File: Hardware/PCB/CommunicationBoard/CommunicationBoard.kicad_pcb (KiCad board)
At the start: 4 copper layers, 60 x 60 mm, 46 parts, among them J1 SWD, J2 Conn_01x07, J3 Conn_01x07, J4 Conn_01x07, J6 USB_C_Receptacle_USB2.0, J7 TWELITER, SW1 nRF_RESET, SW2 nRF_DFU, SW3 TWE_CLEAR, SW4 TWE_RESET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

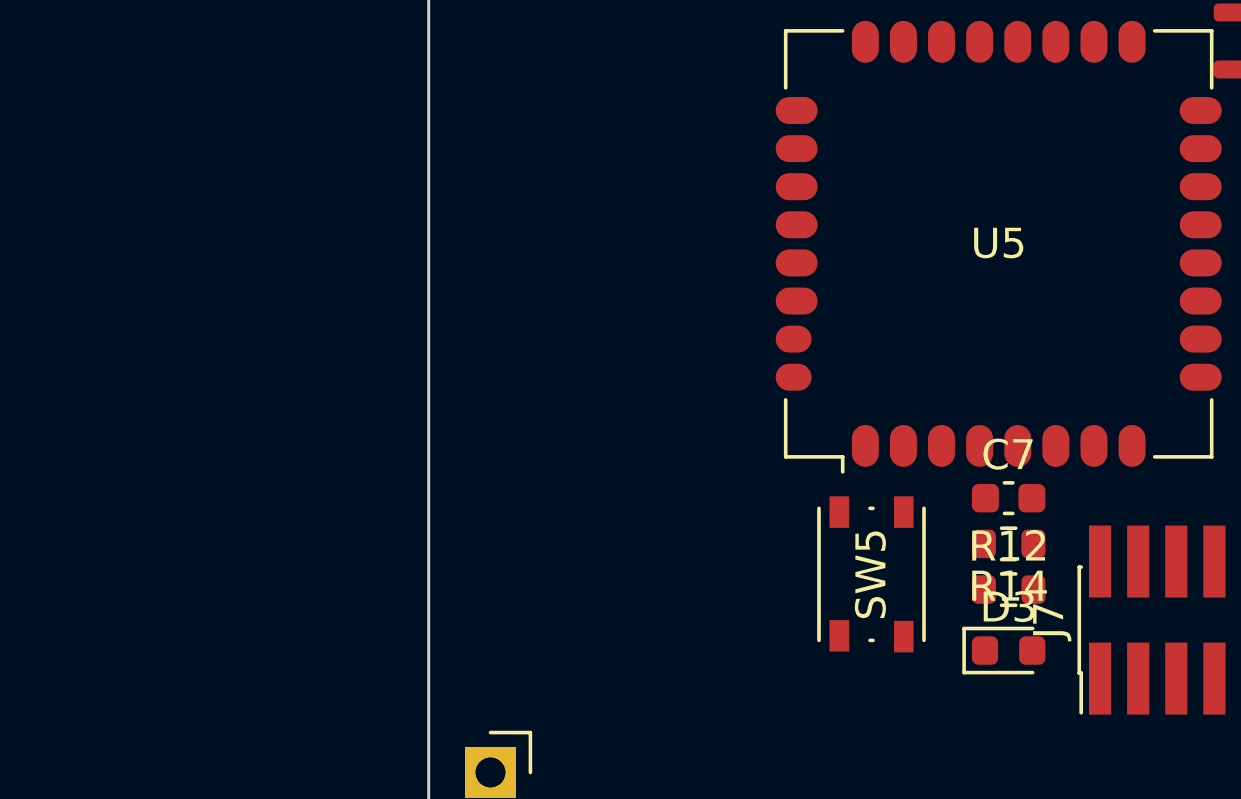
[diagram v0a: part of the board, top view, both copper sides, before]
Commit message: 回路図を微修正、基板を更新済み
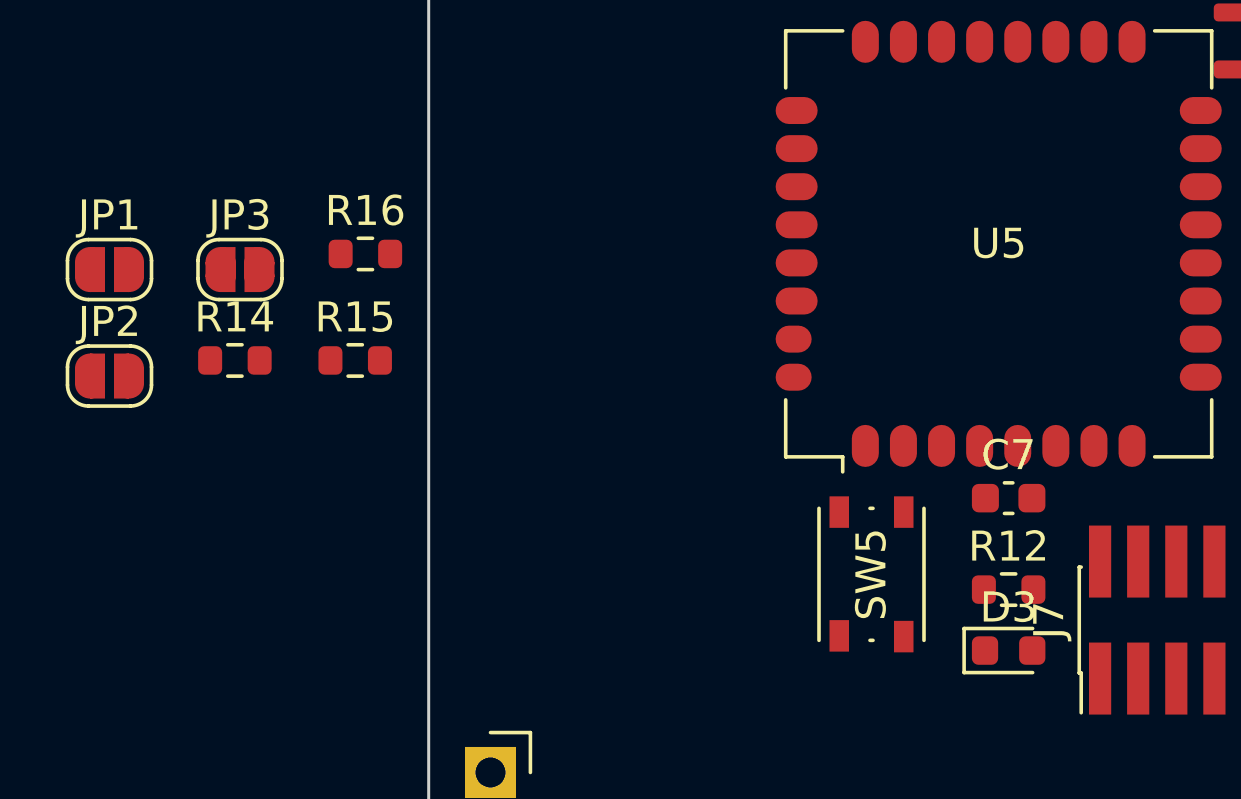
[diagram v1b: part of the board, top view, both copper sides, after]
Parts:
- added JP1: EX1, Jumper:SolderJumper-2_P1.3mm_Open_RoundedPad1.0x1.5mm, F.Cu at (104.4, 90.9)
- added JP2: BPS, Jumper:SolderJumper-2_P1.3mm_Open_RoundedPad1.0x1.5mm, F.Cu at (104.4, 94.4)
- added JP3: SET, Jumper:SolderJumper-2_P1.3mm_Open_RoundedPad1.0x1.5mm, F.Cu at (108.7, 90.9)
- added R15: 10k, Resistor_SMD:R_0603_1608Metric, F.Cu at (112.5, 93.9)
- added R16: DNF, Resistor_SMD:R_0603_1608Metric, F.Cu at (112.9, 90.3)
- moved R14 26.5 mm to (108.5, 93.9), turned to 0 degrees
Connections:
- R14 pad 2: /SPICLK -> /EX1
- U5 pad 1: /SPICLK -> unconnected-(U5-Pad1)
- U5 pad 13: /TWE_SET -> /DIO12
- U5 pad 19: unconnected-(U5-Pad19) -> /BPS
- U5 pad 22: unconnected-(U5-Pad22) -> +3.3V
- U5 pad 23: unconnected-(U5-Pad23) -> +3.3V
- U5 pad 24: unconnected-(U5-Pad24) -> /EX1
- U5 pad 25: unconnected-(U5-Pad25) -> Net-(R15-Pad2)

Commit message: 無線ボード配線7割
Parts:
- added C10: 10μF35V X5R 2012, Capacitor_SMD:C_0805_2012Metric, F.Cu at (134.8, 74.6)
- added C9: 10μF35V X5R 2012, Capacitor_SMD:C_0805_2012Metric, F.Cu at (131.3, 74.6)
- TP1: moved to F.Cu
- moved JP3 34.4 mm to (143.0, 93.4), turned to 90 degrees
- moved JP2 30.0 mm to (127.7, 75.6), turned to 180 degrees
- moved R16 27.7 mm to (138.9, 80.7), turned to 90 degrees
- moved JP1 25.3 mm to (127.7, 81.2)
- moved R14 25.2 mm to (128.5, 78.4), turned to -90 degrees
- moved R15 21.2 mm to (127.0, 78.4), turned to -90 degrees
- moved R10 13.0 mm to (137.4, 78.2), turned to 90 degrees
- moved R2 11.0 mm to (161.9, 83.2), turned to 0 degrees
- moved D2 9.80 mm to (137.4, 75.1)
- moved R1 9.29 mm to (161.9, 81.7), turned to 0 degrees
- moved R13 7.94 mm to (137.4, 80.7), turned to -90 degrees
- moved D3 5.44 mm to (137.6, 99.2), turned to -90 degrees
- moved J7 2.96 mm to (138.4, 105.1)
- moved R12 1.83 mm to (135.3, 100.0)
- moved R11 1.65 mm to (161.9, 84.8)
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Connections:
- J2 pad 1: +5V -> unconnected-(J2-Pad1)
- J3 pad 1: +5V -> unconnected-(J3-Pad1)
- J4 pad 1: +5V -> unconnected-(J4-Pad1)
- U3 pad 12: /SEL0 -> unconnected-(U3-Pad12)
- U3 pad 13: /SEL1 -> unconnected-(U3-Pad13)
- U3 pad 19: unconnected-(U3-Pad19) -> /SEL0
- U3 pad 20: unconnected-(U3-Pad20) -> /SEL1
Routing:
- net +3.3V: track 0.00 -> 50.2 mm, vias 0 -> 5
- net /nRF_RST: track 0.00 -> 41.1 mm, vias 0 -> 2
- net PICO_RX: track 0.00 -> 37.6 mm, vias 0 -> 1
- net PICO_TX: track 0.00 -> 29.1 mm, vias 0 -> 1
- net TWE_TX_SUB: track 7.47 -> 30.8 mm
- net /DFU: track 0.00 -> 23.3 mm, vias 0 -> 2
- net /TWE_SET: track 0.00 -> 18.4 mm
- net /DTR: track 0.00 -> 17.0 mm
- net /SWDIO: track 0.00 -> 15.6 mm, vias 0 -> 2
- net /SWDCLK: track 0.00 -> 15.1 mm, vias 0 -> 2
- net /SEL1: track 0.00 -> 14.0 mm, vias 0 -> 2
- net TWE_RX_SUB: track 0.00 -> 13.9 mm, vias 0 -> 2
- net /TWE_CLR: track 0.00 -> 13.4 mm
- net /SWO: track 0.00 -> 13.0 mm
- net /SEL0: track 0.00 -> 12.2 mm, vias 0 -> 2
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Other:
- board text added: "FLASH CLEAR"
- board text added: "FRST"
- board text added: "SET"

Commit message: 残り未配線23
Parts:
- moved SW5 0.57 mm to (131.3, 100.8)
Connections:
- J3 pad 2: GND -> unconnected-(J3-Pad2)
- J3 pad 3: +3.3V -> unconnected-(J3-Pad3)
- J4 pad 2: GND -> unconnected-(J4-Pad2)
- J4 pad 3: +3.3V -> unconnected-(J4-Pad3)
- U3 pad 13: unconnected-(U3-Pad13) -> /TWE_UART_RTS
- U3 pad 16: /TWE_UART_RTS -> unconnected-(U3-Pad16)
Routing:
- net /TWE_UART_RTS: track 0.00 -> 35.0 mm, vias 0 -> 2
- net /TWE_PRG: track 0.00 -> 10.4 mm
- net GND: vias 30 -> 32
- added copper zone on In2.Cu, net +3.3V
- added copper zone on In1.Cu, net GND
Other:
- board text added: "PRG"

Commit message: 未配線0
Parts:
- added G***: LOGO, LOGO:Logo_takuhoTech, F.Cu at (135.0, 127.5)
- moved R13 7.68 mm to (143.7, 85.0), turned to 0 degrees
- moved JP2 5.59 mm to (127.7, 81.2), turned to 0 degrees
- moved R15 3.89 mm to (127.7, 74.6), turned to 180 degrees
- moved JP1 2.54 mm to (127.7, 78.7)
- moved R14 2.41 mm to (127.7, 76.1), turned to 180 degrees
- moved D2 1.78 mm to (137.4, 76.9)
- moved R10 1.27 mm to (138.1, 79.2), turned to 180 degrees
- moved R16 1.17 mm to (138.1, 81.6), turned to 180 degrees
- moved U7 0.25 mm to (143.0, 83.0)
- moved R9 0.25 mm to (141.2, 79.2)
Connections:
- J2 pad 6: P0.16 -> unconnected-(J2-Pad6)
- J2 pad 7: P0.15 -> unconnected-(J2-Pad7)
- U3 pad 42: P0.16 -> unconnected-(U3-Pad42)
- U3 pad 43: P0.15 -> unconnected-(U3-Pad43)
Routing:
- net /TWE_RST: track 1.61 -> 32.8 mm, vias 1 -> 2
- net +3.3V: track 50.2 -> 79.5 mm
- net /TWE_CLR: track 13.4 -> 31.8 mm
- net /BPS: track 0.00 -> 12.7 mm
- net Net-(R15-Pad2): track 0.00 -> 11.8 mm
- net /EX1: track 0.00 -> 8.24 mm
- net VBUS: track 7.73 -> 14.3 mm
- net Net-(R16-Pad1): track 0.00 -> 4.94 mm
- net Net-(D2-Pad2): track 0.00 -> 1.52 mm
- net GND: vias 32 -> 45
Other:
- board text added: "CLR"
- board text added: "USB"

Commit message: VIA配置中
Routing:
- net GND: vias 45 -> 111
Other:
- board text added: "BPS"
- board text added: "EX1"
